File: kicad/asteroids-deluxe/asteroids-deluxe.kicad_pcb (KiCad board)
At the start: 2 copper layers, 300 x 300 mm, 8 parts

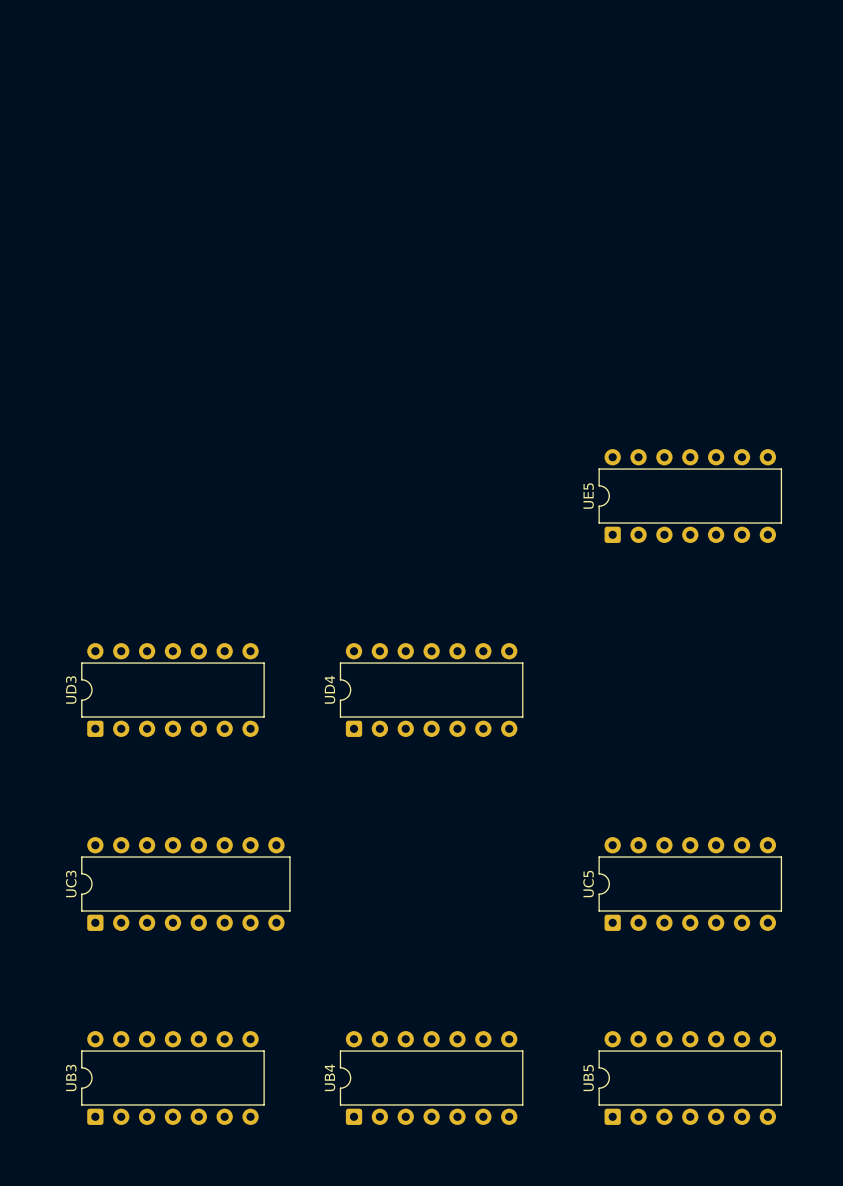
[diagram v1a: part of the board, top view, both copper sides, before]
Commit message: Drop two grid rows that do not exist, and span the devices that do
Atari's grid alphabet skips G, I, O and Q, and the board definitions
listed G and Q as rows. Every device below F was therefore drawn a row
too low, the rendered board carried two empty bands, and F/H1 looked
like a three-position span for a part 1.2in long on a 0.75in pitch.

Confirmed three ways before touching it. Nothing in any read, signature
or signal record in this repo sits in a G or Q row, while both
neighbours of each are populated on the two densest boards — Battlezone
P:6 R:2, Asteroids-03 P:4 R:3. The sheets' own spanning designators
treat F and H as adjacent and H and J as adjacent, which is only
possible if G and I are not positions. And with G removed, F/H falls out
as an adjacent pair, which is what a 24-pin ROM needs. Pong predates the
convention and legitimately uses G, so it keeps its grid.

Spans are now data rather than prose. A device drawn across two or three
cells is still keyed at its first cell, because that is the only thing
`ics` may be keyed by, but the sheet's own designator goes in a `spans`
map and the footprint is placed at the mean of the cells it names. A
DIP-40 at B/C2 sits between B2 and C2 instead of hanging equally over A2
and C2. The build rejects a span whose rows are not adjacent — that
failure almost always means the grid is wrong, not the span.

Two more inconsistencies found and logged rather than guessed at. Two of
the Math Box's four Am2901 slices carry a span and two do not, though
all four are the same DIP-40 on the same pitch. And asteroids-04.json
carries five devices at the -03 PROM positions alongside the -04 ROMs
and is missing 035144-02 at D/E1, contradicting the substitution table,
memory_by_revision and its own status text in the same breath.

Co-Authored-By: Claude Opus 5 <noreply@anthropic.com>
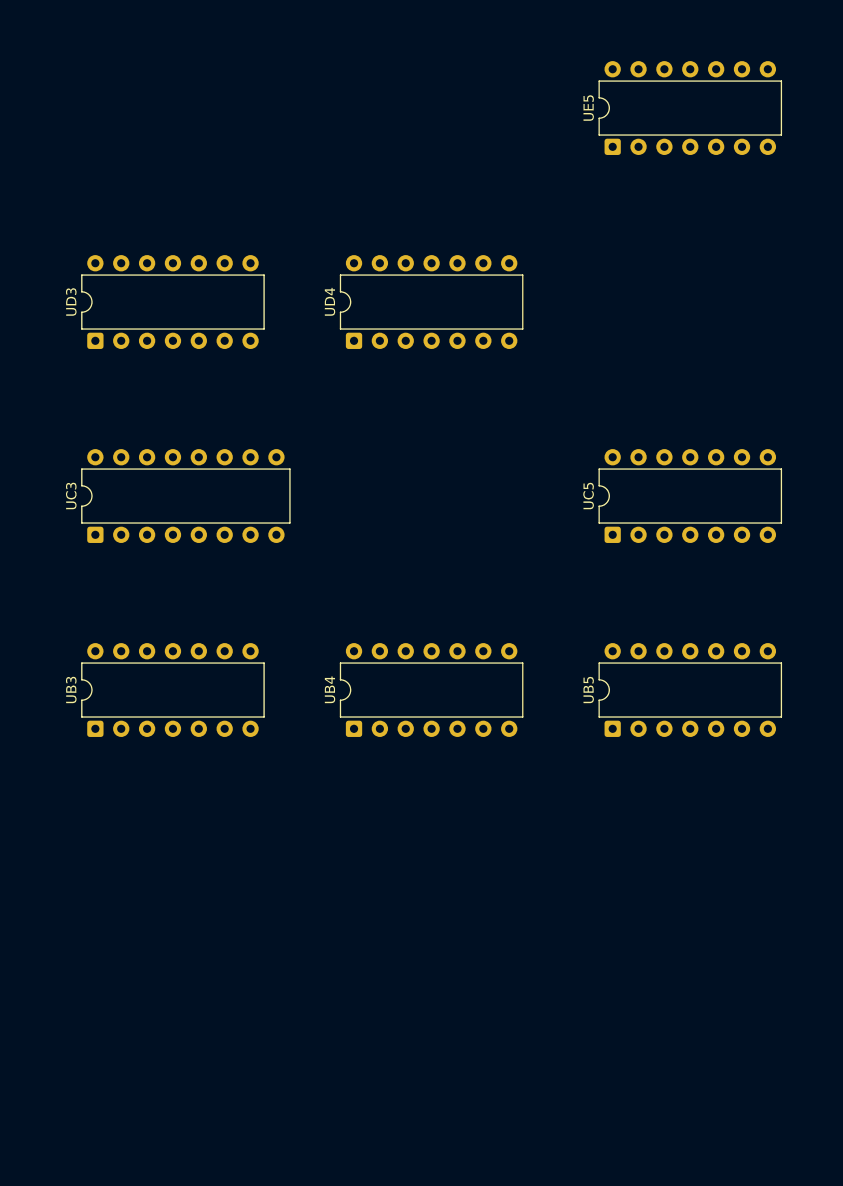
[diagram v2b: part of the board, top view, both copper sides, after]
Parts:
- moved UE5 38.1 mm to (127.6, 189.4)
- moved UB3 38.1 mm to (76.8, 246.6)
- moved UB4 38.1 mm to (102.2, 246.6)
- moved UB5 38.1 mm to (127.6, 246.6)
- moved UD3 38.1 mm to (76.8, 208.5)
- moved UD4 38.1 mm to (102.2, 208.5)
- moved UC3 38.1 mm to (76.8, 227.6)
- moved UC5 38.1 mm to (127.6, 227.6)

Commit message: Take Asteroids Deluxe from 8 devices to 92, and say where each came from
merge_ic_locations.py is the adjudication the parts-list harvest needed.
The drawing read is authoritative wherever it exists, the parts lists
fill the gaps, a device is taken only where two or more printings agree,
and every device records its source — which the chip lookup now shows on
each row.

The two-printing rule matters more than the 85% single-printing figure.
Asteroids Deluxe has four printings; they agree with each other on 100
of 100 designators and with all eight hand-read devices. That is a
different class of evidence, and it is what makes 84 additions
defensible where one printing's word would not be. 66 of them are
attested by four printings and 18 by three.

Nothing was overwritten. The eight devices from the drawing are byte for
byte what they were, now marked as confirmed by the lists rather than
merely asserted.

Three cells are dropped rather than guessed. B10, D10 and F10 are each
claimed twice — a spanning designator from the 74LS157 row against a
plain one from another row — and nothing in the lists says which is
right, so the map has neither. That collision check is the same
discipline the Asteroids revision generator needed: the first run of
this merge silently overwrote all three and would have put a chip on the
map that is not there. Logged; one look at the drawing recovers them.

Two fixes fell out of measuring rather than assuming. A row states its
device twice, as Atari's stock number and in the description, and OCR
rarely mangles both the same way — so the cleaner spelling wins, which
is what turns '741.S157' back into '74LS157'. And device numbers are now
recovered by asking which trailing digits name a part the packaging
table knows, rather than by parsing the family letters that OCR
destroys; that alone took Asteroids Deluxe's cross-printing agreement
from 86 of 100 to 100 of 100.

74LS253 and the parts lists' spelling of the CD4016B join the packaging
table, 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
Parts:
- added UA10: 74LS157, DIP-16_W7.62mm, F.Cu at (254.6, 265.6)
- added UA6: 74LS74, DIP-14_W7.62mm, F.Cu at (153.0, 265.6)
- added UA8: 74LS10, DIP-14_W7.62mm, F.Cu at (203.8, 265.6)
- added UA9: 74LS109, DIP-16_W7.62mm, F.Cu at (229.2, 265.6)
- added UB1: 74LS244, DIP-20_W7.62mm, F.Cu at (26.0, 246.6)
- added UB12: 4016B, DIP-14_W7.62mm, F.Cu at (305.4, 246.6)
- added UB6: 9316, DIP-16_W7.62mm, F.Cu at (153.0, 246.6)
- added UB8: 74LS08, DIP-14_W7.62mm, F.Cu at (203.8, 246.6)
- added UB9: 74LS32, DIP-14_W7.62mm, F.Cu at (229.2, 246.6)
- added UC1: 74LS244, DIP-20_W7.62mm, F.Cu at (26.0, 227.6)
- added UC10: 74LS157, DIP-16_W7.62mm, F.Cu at (254.6, 227.6)
- added UC4: 9316, DIP-16_W7.62mm, F.Cu at (102.2, 227.6)
- added UC6: 9316, DIP-16_W7.62mm, F.Cu at (153.0, 227.6)
- added UC7: 74LS02, DIP-14_W7.62mm, F.Cu at (178.4, 227.6)
- added UC9: 74LS191, DIP-16_W7.62mm, F.Cu at (229.2, 227.6)
- added UD12: 4016B, DIP-14_W7.62mm, F.Cu at (305.4, 208.5)
- added UD5: 74LS02, DIP-14_W7.62mm, F.Cu at (127.6, 208.5)
- added UD6: 74LS161, DIP-16_W7.62mm, F.Cu at (153.0, 208.5)
- added UD8: 74LS174, DIP-16_W7.62mm, F.Cu at (203.8, 208.5)
- added UD9: 74LS191, DIP-16_W7.62mm, F.Cu at (229.2, 208.5)
- added UE10: 74LS157, DIP-16_W7.62mm, F.Cu at (254.6, 189.4)
- added UE2: 74LS245, DIP-20_W7.62mm, F.Cu at (51.4, 189.4)
- added UE3: 74LS139, DIP-16_W7.62mm, F.Cu at (76.8, 189.4)
- added UE4: 74LS20, DIP-14_W7.62mm, F.Cu at (102.2, 189.4)
- added UE6: 74LS42, DIP-16_W7.62mm, F.Cu at (153.0, 189.4)
- added UE8: 74LS42, DIP-16_W7.62mm, F.Cu at (203.8, 189.4)
- added UE9: 74LS191, DIP-16_W7.62mm, F.Cu at (229.2, 189.4)
- added UF2: 74LS157, DIP-16_W7.62mm, F.Cu at (51.4, 170.4)
- added UF3: 74LS670, DIP-16_W7.62mm, F.Cu at (76.8, 170.4)
- added UF4: 74LS193, DIP-16_W7.62mm, F.Cu at (102.2, 170.4)
- added UF5: 74LS157, DIP-16_W7.62mm, F.Cu at (127.6, 170.4)
- added UF6: 74LS273, DIP-20_W7.62mm, F.Cu at (153.0, 170.4)
- added UF8: 7497, DIP-16_W7.62mm, F.Cu at (203.8, 170.4)
- added UF9: 74LS191, DIP-16_W7.62mm, F.Cu at (229.2, 170.4)
- added UH10: 7404, DIP-14_W7.62mm, F.Cu at (254.6, 151.3)
- added UH2: 74LS157, DIP-16_W7.62mm, F.Cu at (51.4, 151.3)
- added UH3: 74LS670, DIP-16_W7.62mm, F.Cu at (76.8, 151.3)
- added UH4: 74LS193, DIP-16_W7.62mm, F.Cu at (102.2, 151.3)
- added UH5: 74LS367, DIP-16_W7.62mm, F.Cu at (127.6, 151.3)
- added UH6: 74LS273, DIP-20_W7.62mm, F.Cu at (153.0, 151.3)
- added UH8: 7497, DIP-16_W7.62mm, F.Cu at (203.8, 151.3)
- added UH9: 74LS191, DIP-16_W7.62mm, F.Cu at (229.2, 151.3)
- added UJ10: 74LS251, DIP-16_W7.62mm, F.Cu at (254.6, 132.3)
- added UJ2: 74LS157, DIP-16_W7.62mm, F.Cu at (51.4, 132.3)
- added UJ3: 74LS670, DIP-16_W7.62mm, F.Cu at (76.8, 132.3)
- added UJ4: 74LS193, DIP-16_W7.62mm, F.Cu at (102.2, 132.3)
- added UJ5: 74LS367, DIP-16_W7.62mm, F.Cu at (127.6, 132.3)
- added UJ6: 74LS273, DIP-20_W7.62mm, F.Cu at (153.0, 132.3)
- added UJ8: 7497, DIP-16_W7.62mm, F.Cu at (203.8, 132.3)
- added UJ9: 74LS191, DIP-16_W7.62mm, F.Cu at (229.2, 132.3)
- added UK2: 74LS157, DIP-16_W7.62mm, F.Cu at (51.4, 113.2)
- added UK4: 74LS191, DIP-16_W7.62mm, F.Cu at (102.2, 113.2)
- added UK5: 74LS08, DIP-14_W7.62mm, F.Cu at (127.6, 113.2)
- added UK6: 74LS273, DIP-20_W7.62mm, F.Cu at (153.0, 113.2)
- added UK8: 7497, DIP-16_W7.62mm, F.Cu at (203.8, 113.2)
- added UK9: 74LS164, DIP-14_W7.62mm, F.Cu at (229.2, 113.2)
- added UL10: 74LS251, DIP-16_W7.62mm, F.Cu at (254.6, 94.2)
- added UL2: 74LS139, DIP-16_W7.62mm, F.Cu at (51.4, 94.2)
- added UL4: 74LS04, DIP-14_W7.62mm, F.Cu at (102.2, 94.2)
- added UL5: 74LS42, DIP-16_W7.62mm, F.Cu at (127.6, 94.2)
- added UL9: 74LS374, DIP-20_W7.62mm, F.Cu at (229.2, 94.2)
- added UM10: 74LS259, DIP-16_W7.62mm, F.Cu at (254.6, 75.2)
- added UM4: 74LS32, DIP-14_W7.62mm, F.Cu at (102.2, 75.2)
- added UM5: 74LS83, DIP-16_W7.62mm, F.Cu at (127.6, 75.2)
- added UM6: 74LS175, DIP-16_W7.62mm, F.Cu at (153.0, 75.2)
- added UM9: 74LS244, DIP-20_W7.62mm, F.Cu at (229.2, 75.2)
- added UN10: 74LS174, DIP-16_W7.62mm, F.Cu at (254.6, 56.1)
- added UN4: 74LS00, DIP-14_W7.62mm, F.Cu at (102.2, 56.1)
- added UN5: 74LS32, DIP-14_W7.62mm, F.Cu at (127.6, 56.1)
- added UN6: 7406, DIP-14_W7.62mm, F.Cu at (153.0, 56.1)
- added UN8: 74LS10, DIP-14_W7.62mm, F.Cu at (203.8, 56.1)
- added UP1: 74LS245, DIP-20_W7.62mm, F.Cu at (26.0, 37.0)
- added UP10: 74LS02, DIP-14_W7.62mm, F.Cu at (254.6, 37.0)
- added UP4: 74LS86, DIP-14_W7.62mm, F.Cu at (102.2, 37.0)
- added UP5: 74LS253, DIP-16_W7.62mm, F.Cu at (127.6, 37.0)
- added UP6: 74LS174, DIP-16_W7.62mm, F.Cu at (153.0, 37.0)
- added UP7: 9316, DIP-16_W7.62mm, F.Cu at (178.4, 37.0)
- added UP8: 74LS164, DIP-14_W7.62mm, F.Cu at (203.8, 37.0)
- added UP9: 74LS175, DIP-16_W7.62mm, F.Cu at (229.2, 37.0)
- added UR11: 4016B, DIP-14_W7.62mm, F.Cu at (280.0, 18.0)
- added UR6: 74LS08, DIP-14_W7.62mm, F.Cu at (153.0, 18.0)
- added UR7: 74LS74, DIP-14_W7.62mm, F.Cu at (178.4, 18.0)
- added UR8: 74LS164, DIP-14_W7.62mm, F.Cu at (203.8, 18.0)
- added UR9: 74LS04, DIP-14_W7.62mm, F.Cu at (229.2, 18.0)

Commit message: Place the memory devices the IC parts lists cannot reach
Atari stocks ROM, RAM and the microprocessor under its own part numbers
— 90-7033, 036175-01, 90-6013 — not as 37-series IC stock, so the IC
harvest cannot see them however well it reads. That is why Centipede's
ROMs were missing and Red Baron's map had ten devices. merge_memory.py
reads those rows from the same typeset parts lists, under the same rules
as the IC merge: the drawing wins where it exists, two documents must
agree, and nothing is placed whose package cannot be established.

Red Baron 10 to 15, Asteroids Deluxe 92 to 100, Tempest 83 to 88,
Centipede 93 to 95, Missile Command 83 to 85, Lunar Lander 60 to 62.
1,494 devices across the boards, all sized, none contradicted.

Establishing the packages took two corrections, and both were the same
mistake in different clothes.

The first attempt sized Atari stock numbers by correlating a part
against the contact count of the socket at the positions it occupies,
pooled across a machine's documents. That is not a near miss: it put the
2114 at 40 pins, on twelve positions of apparent evidence, because two
printings number the board differently and the correlation was reading
one printing's parts list against another's sockets. Confined to within
a single document it behaves — 33 stock numbers established, 90-6013 by
39 documents agreeing, and 90-7033 correctly refusing to answer rather
than answering wrongly. Those 33 are in packages.py with their
provenance.

The second was the same shape. MAME's dump size was sizing a part from
whatever MAME dumped at that cell, which on Red Baron meant sizing
036175-01 from a dump of 037000-01 — sizing the socket, not the chip.
MAME now sizes a part only when the dump is of that part. Red Baron
loses two devices and keeps thirteen that are right.

Four more parts are sized from MAME's dump sizes alone, where every set
carrying the part agrees and the era leaves no room: 32 bytes and 256
bytes are both bipolar PROMs in a 1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
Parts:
- added UC2: 90-6013, DIP-40_W15.24mm, F.Cu at (51.4, 227.6)
- added UC8: 034602-01, DIP-16_W7.62mm, F.Cu at (203.8, 227.6)
- added UD1: 036430-01, DIP-24_W15.24mm, F.Cu at (26.0, 208.5)
- added UE1: 036431-01, DIP-24_W15.24mm, F.Cu at (26.0, 179.9)
- added UH1: 036432-01, DIP-24_W15.24mm, F.Cu at (26.0, 151.3)
- added UJ1: 036433-02, DIP-24_W15.24mm, F.Cu at (26.0, 132.3)
- added UN2: 036799-01, DIP-24_W15.24mm, F.Cu at (51.4, 46.6)
- added UR2: 036800-01, DIP-24_W15.24mm, F.Cu at (51.4, 18.0)

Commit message: Put MAME's ROM positions on the maps; let the late Asteroids boards take the lists
Two things declined earlier as decisions rather than chores, reconsidered.

The parts-list harvest never reaches memory. Atari stocks ROMs and PROMs under
its own part numbers, not as 37-series IC stock, so those rows fail the
checksum the harvest depends on — which is why Red Baron's whole complement was
missing once, and why 79 memory cells on 15 boards sat empty with everything
around them filled. MAME has them: its ROM file names encode the board
position — 035224.e2 is part 035224 at E2, 037587-01.fh1 is at the span F/H1 —
and they were checked against real boards by the people who dumped them. The
site already publishes those maps as their own asset with their own caveat.
This is that source reaching the board map under the same label, not a new one
mixed in quietly: 78 devices on 14 boards, each recorded in the chip lookup as
"MAME ROM map", only where the map had nothing. The three cells where a parts
list and MAME disagree are untouched and stay logged.

Asteroids -05 and -06 were left without the parts lists because those are
written in early designators and a direct merge would put a device one column
from where the board has it. So they take -03's parts-list additions instead,
shifted through the drawing's early-to-late table where an alternate is known
and placed at the early cell otherwise — which is exactly what these boards
already do for their 78 unshifted drawing-read devices, under a caveat they
already carry. 13 each. None of the 22 turned out to have a known alternate,
and 9 land on cells a shifted device already occupies and are skipped rather
than duplicated. All of it runs inside the generator, so it survives
regeneration.

50 boards, 2,672 devices.

Co-Authored-By: Claude Fable 5.1 <noreply@anthropic.com>
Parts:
- added UF1: 036432-02, DIP-14_W7.62mm, F.Cu at (26.0, 160.9)
